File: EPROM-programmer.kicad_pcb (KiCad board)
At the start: 2 copper layers, 139.7 x 139.7 mm, 90 parts, among them J1 ZIF-socket, J10 VCC, J2 ISP, J5 GND, J6 Barrel_Jack_Switch, J7 ZIF_VCC, J8 VPP, J9 GND, P1 USB-C, Q1 BC327, Q2 BC327, Q3 BC327, Q4 BC327, Q5 BC327, Q6 BC327, SW1 Reset, U1 ATmega1284-P, U2 MCP2221AxP, U3 MCP4812, U4 LM358, U5 ULN2003, U6 LM317_TO-220, U7 LM317_TO-220, U8 LM7805_TO220, U9 MC34063AP, Y1 20M

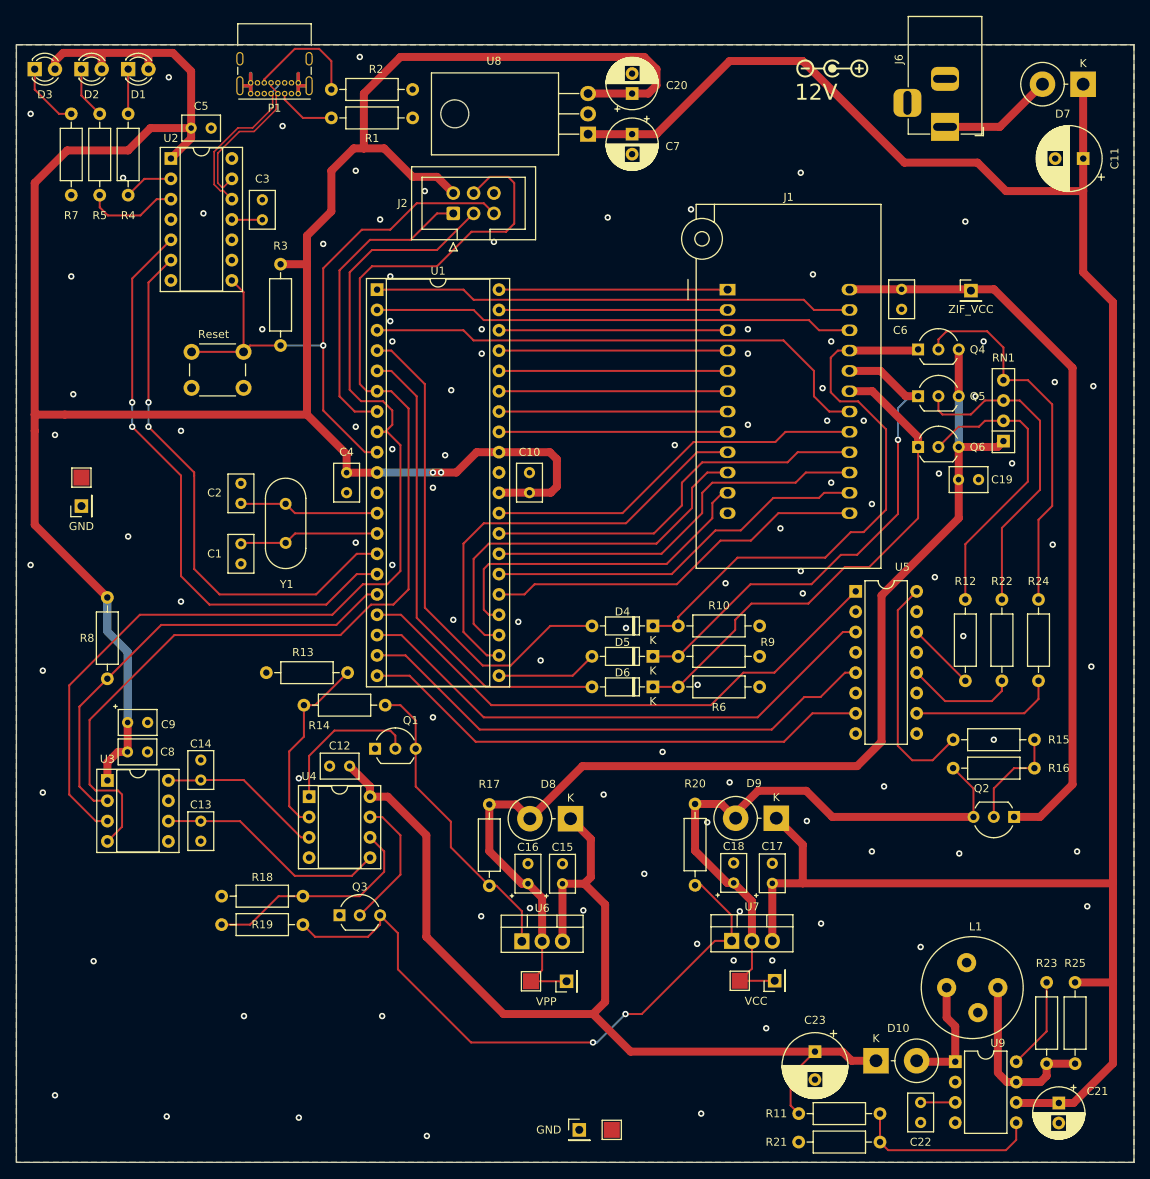
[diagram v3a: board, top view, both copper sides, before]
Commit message: Add input/output protection on data lines (WIP)
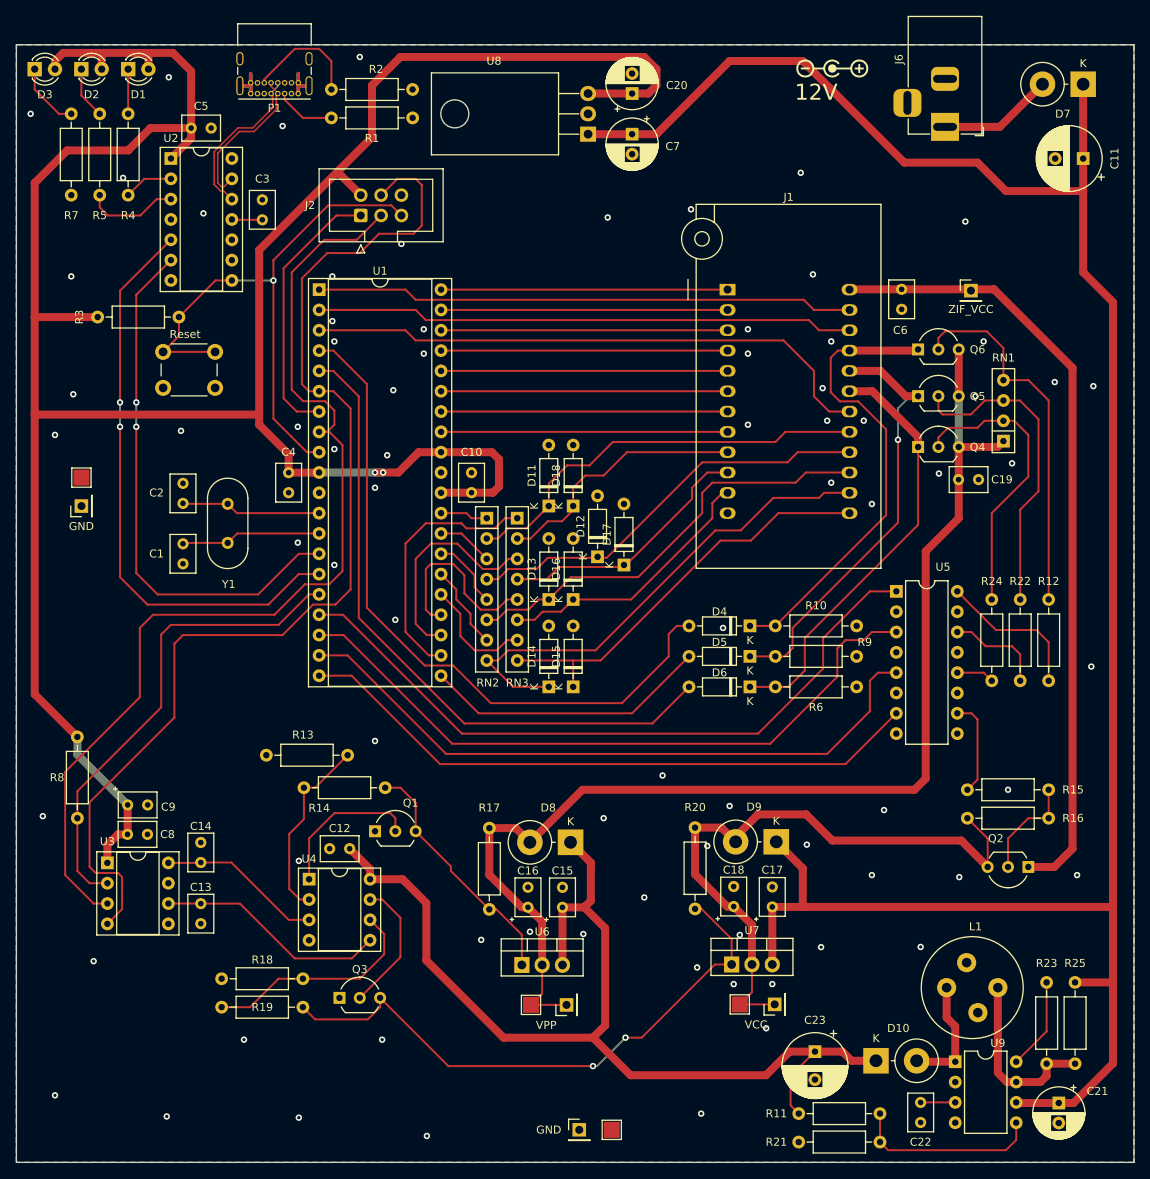
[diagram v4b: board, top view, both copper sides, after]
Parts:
- added D11: 4v7, Diode_THT:D_DO-35_SOD27_P7.62mm_Horizontal, F.Cu at (85.6, 95.8)
- added D12: 4v7, Diode_THT:D_DO-35_SOD27_P7.62mm_Horizontal, F.Cu at (91.7, 102.1)
- added D13: 4v7, Diode_THT:D_DO-35_SOD27_P7.62mm_Horizontal, F.Cu at (85.6, 107.4)
- added D14: 4v7, Diode_THT:D_DO-35_SOD27_P7.62mm_Horizontal, F.Cu at (85.6, 118.4)
- added D15: 4v7, Diode_THT:D_DO-35_SOD27_P7.62mm_Horizontal, F.Cu at (88.6, 118.4)
- added D16: 4v7, Diode_THT:D_DO-35_SOD27_P7.62mm_Horizontal, F.Cu at (88.6, 107.4)
- added D17: 4v7, Diode_THT:D_DO-35_SOD27_P7.62mm_Horizontal, F.Cu at (95.0, 103.1)
- added D18: 4v7, Diode_THT:D_DO-35_SOD27_P7.62mm_Horizontal, F.Cu at (88.6, 95.8)
- added RN2: R_Pack04_SIP_Split, Resistor_THT:R_Array_SIP8, F.Cu at (77.8, 97.3)
- added RN3: R_Pack04_SIP_Split, Resistor_THT:R_Array_SIP8, F.Cu at (81.7, 97.3)
- moved R3 23.8 mm to (29.2, 72.1), turned to 0 degrees
- moved R8 17.8 mm to (26.7, 124.6)
- moved Q4 12.2 mm to (131.8, 88.4)
- moved Q6 12.2 mm to (131.8, 76.2)
- moved D4 12.1 mm to (110.7, 110.7)
- moved D5 12.1 mm to (110.7, 114.6)
- moved D6 12.1 mm to (110.7, 118.4)
- moved R10 12.1 mm to (113.9, 110.7)
- moved R6 12.1 mm to (113.9, 118.4)
- moved R9 12.1 mm to (113.9, 114.6)
- moved J2 11.6 mm to (62.1, 59.4)
- moved R12 10.4 mm to (148.1, 107.4)
- moved R19 10.3 mm to (44.7, 158.4)
- moved R13 10.3 mm to (50.3, 126.9)
- moved C12 10.3 mm to (60.7, 138.6)
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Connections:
- net Net-(Q5-B) renamed /Programmer/NPN_BASE_P20
- C13 pad 1: /Power/DAC_VCC -> Net-(U3-VB)
- C14 pad 1: /Power/DAC_VPP -> /Power/DAC_VCC
- Q4 pad 1: /Programmer/ZIF_P21 -> /Programmer/ZIF_P19
- Q4 pad 2: Net-(Q4-B) -> /Programmer/NPN_BASE_P19
- Q6 pad 1: /Programmer/ZIF_P19 -> /Programmer/ZIF_P21
- Q6 pad 2: Net-(Q6-B) -> /Programmer/NPN_BASE_P21
- R12 pad 1: Net-(Q6-B) -> /Programmer/NPN_BASE_P21
- R12 pad 2: /Programmer/~{ZIF_VPP_P19_EN} -> /Programmer/~{ZIF_VPP_P21_EN}
- R24 pad 1: Net-(Q4-B) -> /Programmer/NPN_BASE_P19
- R24 pad 2: /Programmer/~{ZIF_VPP_P21_EN} -> /Programmer/~{ZIF_VPP_P19_EN}
- RN1 pad 2: Net-(Q6-B) -> /Programmer/NPN_BASE_P19
- RN1 pad 4: Net-(Q4-B) -> /Programmer/NPN_BASE_P21
- U1 pad 17: /Programmer/ZIF_VCC_EN -> /Programmer/ZIF_VPP_P21_EN
- U1 pad 18: /Programmer/ZIF_VPP_P19_EN -> /Programmer/ZIF_VPP_P20_EN
- U1 pad 19: /Programmer/ZIF_VPP_P20_EN -> /Programmer/ZIF_VPP_P19_EN
- U1 pad 20: /Programmer/ZIF_VPP_P21_EN -> /Programmer/ZIF_VCC_EN
- U1 pad 22: /Programmer/ZIF_P9 -> Net-(RN3A-R1.1)
- U1 pad 23: /Programmer/ZIF_P10 -> Net-(RN3B-R2.1)
- U1 pad 24: /Programmer/ZIF_P11 -> Net-(RN3C-R3.1)
- U1 pad 25: /Programmer/ZIF_P13 -> Net-(RN3D-R4.1)
- U1 pad 26: /Programmer/ZIF_P14 -> Net-(RN2D-R4.1)
- U1 pad 27: /Programmer/ZIF_P15 -> Net-(RN2C-R3.1)
- U1 pad 28: /Programmer/ZIF_P16 -> Net-(RN2B-R2.1)
- U1 pad 29: /Programmer/ZIF_P17 -> Net-(RN2A-R1.1)
- U3 pad 6: /Power/DAC_VCC -> Net-(U3-VB)
- U3 pad 8: /Power/DAC_VPP -> /Power/DAC_VCC
- U4 pad 3: /Power/DAC_VPP -> /Power/DAC_VCC
- U4 pad 5: /Power/DAC_VCC -> Net-(U3-VB)
- U5 pad 1: /Programmer/ZIF_VCC_EN -> /Programmer/ZIF_VPP_P21_EN
- U5 pad 10: /Programmer/~{ZIF_VPP_P21_EN} -> /Programmer/~{ZIF_VCC_EN}
- U5 pad 12: /Programmer/~{ZIF_VPP_P20_EN} -> /Programmer/~{ZIF_VPP_P19_EN}
- U5 pad 14: /Programmer/~{ZIF_VPP_P19_EN} -> /Programmer/~{ZIF_VPP_P20_EN}
- U5 pad 16: /Programmer/~{ZIF_VCC_EN} -> /Programmer/~{ZIF_VPP_P21_EN}
- U5 pad 3: /Programmer/ZIF_VPP_P19_EN -> /Programmer/ZIF_VPP_P20_EN
- U5 pad 5: /Programmer/ZIF_VPP_P20_EN -> /Programmer/ZIF_VPP_P19_EN
- U5 pad 7: /Programmer/ZIF_VPP_P21_EN -> /Programmer/ZIF_VCC_EN
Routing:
- net Net-(Q4-B): track 47.2 -> 0.00 mm
- net /Programmer/NPN_BASE_P21: track 0.00 -> 46.4 mm
- net Net-(Q6-B): track 37.5 -> 0.00 mm
- net /Programmer/NPN_BASE_P19: track 0.00 -> 36.5 mm
- net Net-(RN3A-R1.1): track 0.00 -> 32.0 mm
- net Net-(U3-VB): track 0.00 -> 29.0 mm
- net Net-(RN3B-R2.1): track 0.00 -> 26.7 mm
- net /Programmer/D_P21: track 61.6 -> 86.5 mm
- net /Programmer/D_P20: track 12.6 -> 35.9 mm
- net /Programmer/ZIF_VPP_P21_EN: track 64.7 -> 87.9 mm
- net /Programmer/D_P19: track 59.4 -> 82.6 mm
- net Net-(RN3C-R3.1): track 0.00 -> 22.7 mm
- net /Programmer/ZIF_P9: track 54.5 -> 32.4 mm
- net /Power/DAC_VPP: track 20.6 -> 0.00 mm
- net /Programmer/ZIF_VPP_P20_EN: track 66.6 -> 85.6 mm
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
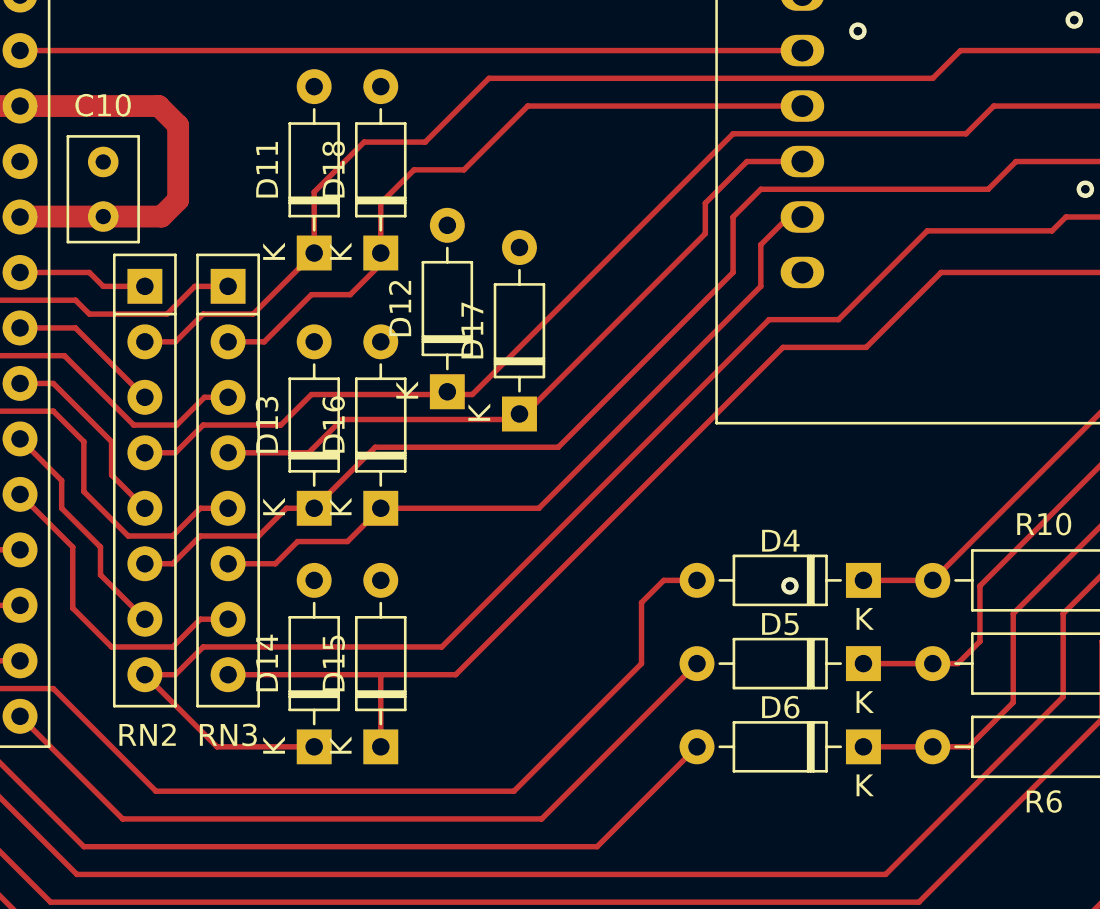
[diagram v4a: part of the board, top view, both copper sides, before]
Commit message: Add input/output protection on data lines (WIP)
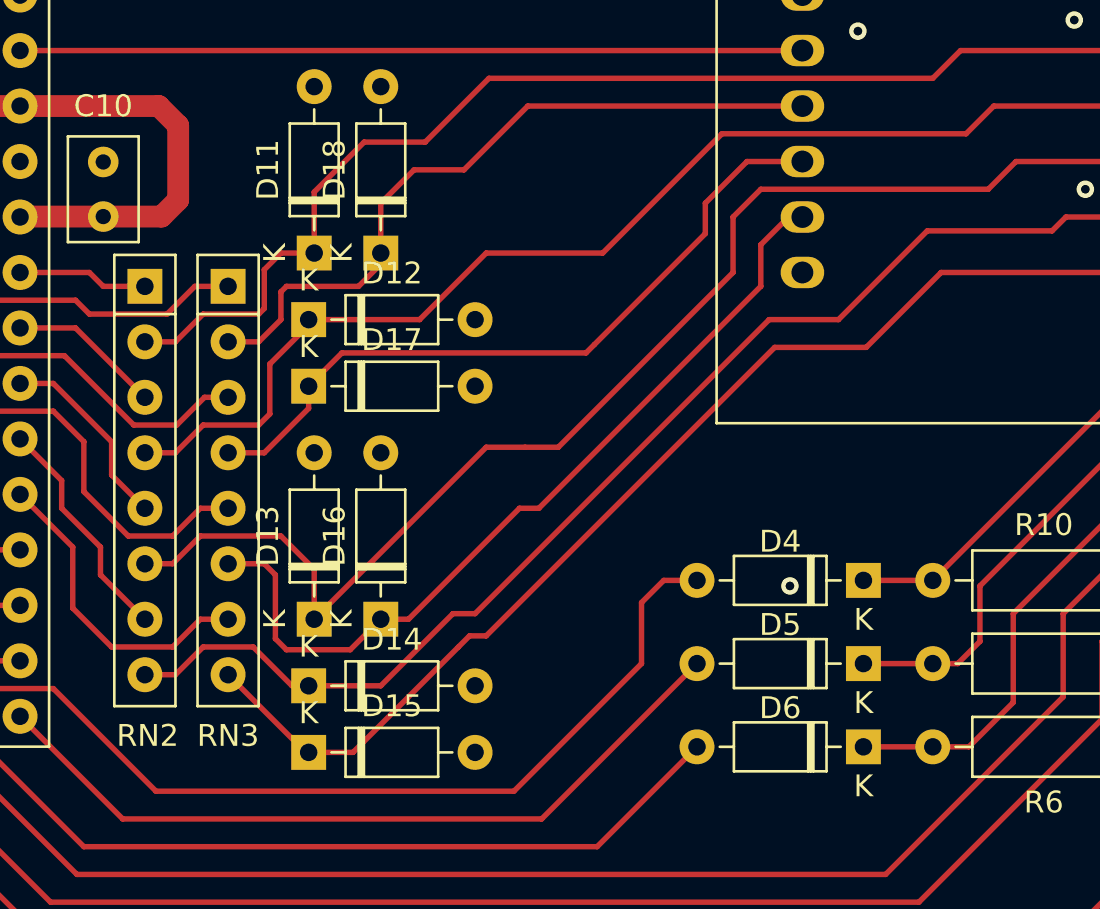
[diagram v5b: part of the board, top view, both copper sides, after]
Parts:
- moved D17 9.74 mm to (85.3, 101.9), turned to 0 degrees
- moved D12 7.16 mm to (85.3, 98.8), turned to 0 degrees
- moved D13 5.08 mm to (85.6, 112.5)
- moved D16 5.08 mm to (88.6, 112.5)
- moved D15 3.31 mm to (85.3, 118.6), turned to 0 degrees
- moved D14 2.81 mm to (85.3, 115.6), turned to 0 degrees
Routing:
- net /Programmer/ZIF_P14: track 63.7 -> 56.0 mm
- net /Programmer/ZIF_P11: track 34.0 -> 39.0 mm
- net /Programmer/ZIF_P15: track 55.0 -> 59.5 mm
- net /Programmer/ZIF_P16: track 52.4 -> 53.9 mm
- net /Programmer/ZIF_P17: track 53.0 -> 54.1 mm
- net /Programmer/ZIF_P9: track 32.4 -> 33.1 mm
- net /Programmer/ZIF_P10: track 32.6 -> 33.2 mm
- net /Programmer/ZIF_P13: track 52.5 -> 53.0 mm

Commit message: Clean up of schematic
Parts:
- RN2, RN3: value R_Pack04_SIP_Split -> 120
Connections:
- net /Programmer/D_P19 renamed /Programmer/MCU_P19
- net /Programmer/D_P20 renamed /Programmer/MCU_P20
- net /Programmer/D_P21 renamed /Programmer/MCU_P21
- net Net-(RN2A-R1.1) renamed /Programmer/MCU_P17
- net Net-(RN2B-R2.1) renamed /Programmer/MCU_P16
- net Net-(RN2C-R3.1) renamed /Programmer/MCU_P15
- net Net-(RN2D-R4.1) renamed /Programmer/MCU_P14
- net Net-(RN3A-R1.1) renamed /Programmer/MCU_P9
- net Net-(RN3B-R2.1) renamed /Programmer/MCU_P10
- net Net-(RN3C-R3.1) renamed /Programmer/MCU_P11
- net Net-(RN3D-R4.1) renamed /Programmer/MCU_P13
- C13 pad 1: Net-(U3-VB) -> /Power/DAC_VCC
- C14 pad 1: /Power/DAC_VCC -> /Power/DAC_VPP
- U3 pad 6: Net-(U3-VB) -> /Power/DAC_VCC
- U3 pad 8: /Power/DAC_VCC -> /Power/DAC_VPP
- U4 pad 3: /Power/DAC_VCC -> /Power/DAC_VPP
- U4 pad 5: Net-(U3-VB) -> /Power/DAC_VCC
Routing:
- net Net-(U3-VB): track 29.0 -> 0.00 mm
- net /Power/DAC_VPP: track 0.00 -> 20.6 mm
- net /Power/DAC_VCC: track 20.6 -> 29.0 mm
